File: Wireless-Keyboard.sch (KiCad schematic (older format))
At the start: 24 parts, among them SW1 SW_Push, U1 ATmega32U4-AU, Y1 16MHz

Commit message: schematic matrix done
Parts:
- added D? (x76): D_Small, Diode_SMD:D_SOD-123, symbol Device:D_Small
- added MX?: 2, MX_Only:MXOnly-1U-NoLED, symbol MX_Alps_Hybrid:MX-NoLED
- added MX?: W, MX_Only:MXOnly-1U-NoLED, symbol MX_Alps_Hybrid:MX-NoLED
- added MX?: 3, MX_Only:MXOnly-1U-NoLED, symbol MX_Alps_Hybrid:MX-NoLED
- added MX?: E, MX_Only:MXOnly-1U-NoLED, symbol MX_Alps_Hybrid:MX-NoLED
- added MX?: 4, MX_Only:MXOnly-1U-NoLED, symbol MX_Alps_Hybrid:MX-NoLED
- added MX?: R, MX_Only:MXOnly-1U-NoLED, symbol MX_Alps_Hybrid:MX-NoLED
- added MX?: 5, MX_Only:MXOnly-1U-NoLED, symbol MX_Alps_Hybrid:MX-NoLED
- added MX?: T, MX_Only:MXOnly-1U-NoLED, symbol MX_Alps_Hybrid:MX-NoLED
- added MX?: 6, MX_Only:MXOnly-1U-NoLED, symbol MX_Alps_Hybrid:MX-NoLED
- added MX?: Y, MX_Only:MXOnly-1U-NoLED, symbol MX_Alps_Hybrid:MX-NoLED
- added MX?: 7, MX_Only:MXOnly-1U-NoLED, symbol MX_Alps_Hybrid:MX-NoLED
- added MX?: U, MX_Only:MXOnly-1U-NoLED, symbol MX_Alps_Hybrid:MX-NoLED
- added MX?: 8, MX_Only:MXOnly-1U-NoLED, symbol MX_Alps_Hybrid:MX-NoLED
- added MX?: I, MX_Only:MXOnly-1U-NoLED, symbol MX_Alps_Hybrid:MX-NoLED
- added MX?: 9, MX_Only:MXOnly-1U-NoLED, symbol MX_Alps_Hybrid:MX-NoLED
- added MX?: O, MX_Only:MXOnly-1U-NoLED, symbol MX_Alps_Hybrid:MX-NoLED
- added MX?: 0, MX_Only:MXOnly-1U-NoLED, symbol MX_Alps_Hybrid:MX-NoLED
- added MX?: P, MX_Only:MXOnly-1U-NoLED, symbol MX_Alps_Hybrid:MX-NoLED
- added MX?: -_, MX_Only:MXOnly-1U-NoLED, symbol MX_Alps_Hybrid:MX-NoLED
- added MX?: [{, MX_Only:MXOnly-1U-NoLED, symbol MX_Alps_Hybrid:MX-NoLED
- added MX?: =+, MX_Only:MXOnly-1U-NoLED, symbol MX_Alps_Hybrid:MX-NoLED
- added MX?: ]}, MX_Only:MXOnly-1U-NoLED, symbol MX_Alps_Hybrid:MX-NoLED
- added MX?: Backspace 2u, MX_Only:MXOnly-1U-NoLED, symbol MX_Alps_Hybrid:MX-NoLED
- added MX?: Blank 3 1.5u, MX_Only:MXOnly-1U-NoLED, symbol MX_Alps_Hybrid:MX-NoLED
- added MX?: Blank 1 1u, MX_Only:MXOnly-1U-NoLED, symbol MX_Alps_Hybrid:MX-NoLED
- added MX? (x7): MX-NoLED, MX_Only:MXOnly-1U-NoLED, symbol MX_Alps_Hybrid:MX-NoLED
- added MX?: Blank 2 1u, MX_Only:MXOnly-1U-NoLED, symbol MX_Alps_Hybrid:MX-NoLED
- added MX?: A, MX_Only:MXOnly-1U-NoLED, symbol MX_Alps_Hybrid:MX-NoLED
- added MX?: CAPS 1.75u, MX_Only:MXOnly-1U-NoLED, symbol MX_Alps_Hybrid:MX-NoLED
- added MX?: S, MX_Only:MXOnly-1U-NoLED, symbol MX_Alps_Hybrid:MX-NoLED
- added MX?: D, MX_Only:MXOnly-1U-NoLED, symbol MX_Alps_Hybrid:MX-NoLED
- added MX?: F, MX_Only:MXOnly-1U-NoLED, symbol MX_Alps_Hybrid:MX-NoLED
- added MX?: G, MX_Only:MXOnly-1U-NoLED, symbol MX_Alps_Hybrid:MX-NoLED
- added MX?: H, MX_Only:MXOnly-1U-NoLED, symbol MX_Alps_Hybrid:MX-NoLED
- added MX?: J, MX_Only:MXOnly-1U-NoLED, symbol MX_Alps_Hybrid:MX-NoLED
- added MX?: K, MX_Only:MXOnly-1U-NoLED, symbol MX_Alps_Hybrid:MX-NoLED
- added MX?: L, MX_Only:MXOnly-1U-NoLED, symbol MX_Alps_Hybrid:MX-NoLED
- added MX?: ;:, MX_Only:MXOnly-1U-NoLED, symbol MX_Alps_Hybrid:MX-NoLED
- added MX?: @', MX_Only:MXOnly-1U-NoLED, symbol MX_Alps_Hybrid:MX-NoLED
- added MX?: Blank 4 2.25u, MX_Only:MXOnly-1U-NoLED, symbol MX_Alps_Hybrid:MX-NoLED
- added MX?: tilda#, MX_Only:MXOnly-1U-NoLED, symbol MX_Alps_Hybrid:MX-NoLED
- added MX?: ENTER ISO, MX_Only:MXOnly-1U-NoLED, symbol MX_Alps_Hybrid:MX-NoLED
- added MX?: \\|, MX_Only:MXOnly-1U-NoLED, symbol MX_Alps_Hybrid:MX-NoLED
- added MX?: LShift 1.25u, MX_Only:MXOnly-1U-NoLED, symbol MX_Alps_Hybrid:MX-NoLED
- added MX?: Blank 5 2.25u, MX_Only:MXOnly-1U-NoLED, symbol MX_Alps_Hybrid:MX-NoLED
- added MX?: Z, MX_Only:MXOnly-1U-NoLED, symbol MX_Alps_Hybrid:MX-NoLED
- added MX?: X, MX_Only:MXOnly-1U-NoLED, symbol MX_Alps_Hybrid:MX-NoLED
- added MX?: C, MX_Only:MXOnly-1U-NoLED, symbol MX_Alps_Hybrid:MX-NoLED
- added MX?: V, MX_Only:MXOnly-1U-NoLED, symbol MX_Alps_Hybrid:MX-NoLED
- added MX?: B, MX_Only:MXOnly-1U-NoLED, symbol MX_Alps_Hybrid:MX-NoLED
- added MX?: N, MX_Only:MXOnly-1U-NoLED, symbol MX_Alps_Hybrid:MX-NoLED
- added MX?: M, MX_Only:MXOnly-1U-NoLED, symbol MX_Alps_Hybrid:MX-NoLED
- added MX?: <,, MX_Only:MXOnly-1U-NoLED, symbol MX_Alps_Hybrid:MX-NoLED
- added MX?: .>, MX_Only:MXOnly-1U-NoLED, symbol MX_Alps_Hybrid:MX-NoLED
- added MX?: /?, MX_Only:MXOnly-1U-NoLED, symbol MX_Alps_Hybrid:MX-NoLED
- added MX?: RShift 2.75U, MX_Only:MXOnly-1U-NoLED, symbol MX_Alps_Hybrid:MX-NoLED
- added MX?: WIN 1.25U, MX_Only:MXOnly-1U-NoLED, symbol MX_Alps_Hybrid:MX-NoLED
- added MX?: LCTRL 1.25U, MX_Only:MXOnly-1U-NoLED, symbol MX_Alps_Hybrid:MX-NoLED
- added MX?: ALT 1.25U, MX_Only:MXOnly-1U-NoLED, symbol MX_Alps_Hybrid:MX-NoLED
- added MX? (x6): ***, MX_Only:MXOnly-1U-NoLED, symbol MX_Alps_Hybrid:MX-NoLED
- added MX?: SPACEBAR 6.25U, MX_Only:MXOnly-1U-NoLED, symbol MX_Alps_Hybrid:MX-NoLED
- added MX?: ALTGR 1.25u, MX_Only:MXOnly-1U-NoLED, symbol MX_Alps_Hybrid:MX-NoLED
- added MX?: WIN 1.25u, MX_Only:MXOnly-1U-NoLED, symbol MX_Alps_Hybrid:MX-NoLED
- added MX?: FN 1.25U, MX_Only:MXOnly-1U-NoLED, symbol MX_Alps_Hybrid:MX-NoLED
- added MX?: RCTRL 1.25u, MX_Only:MXOnly-1U-NoLED, symbol MX_Alps_Hybrid:MX-NoLED
- MX1: value MX-NoLED -> ESC; footprint (none) -> MX_Only:MXOnly-1U-NoLED
- MX2: value MX-NoLED -> Tab 1.5u; footprint (none) -> MX_Only:MXOnly-1U-NoLED
- MX3: value MX-NoLED -> 1; footprint (none) -> MX_Only:MXOnly-1U-NoLED
- MX4: value MX-NoLED -> Q; footprint (none) -> MX_Only:MXOnly-1U-NoLED
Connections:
- net labels added: COL10, COL11, COL12, COL13, COL14, COL15, COL2, COL3, COL4, COL5, COL6, COL7, COL8, COL9, ROW2, ROW3, ROW4
- wire segments 58 -> 286
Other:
- moved on the sheet: C1, C2, C3, C4, C5, C6, C7, D3, D4, MX3, MX4, R1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

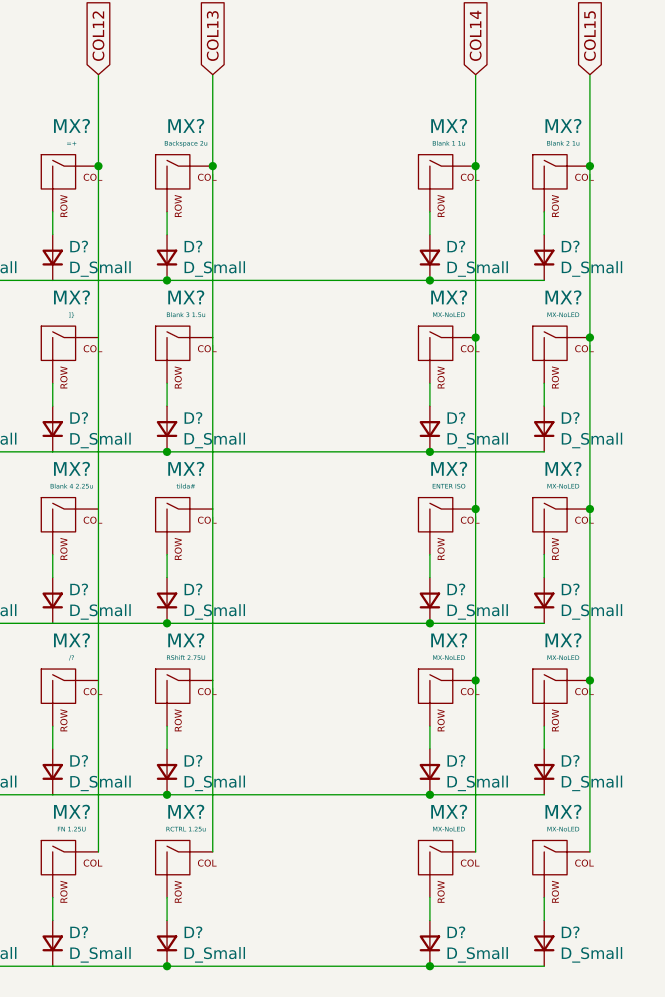
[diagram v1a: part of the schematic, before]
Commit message: Schematic redraw
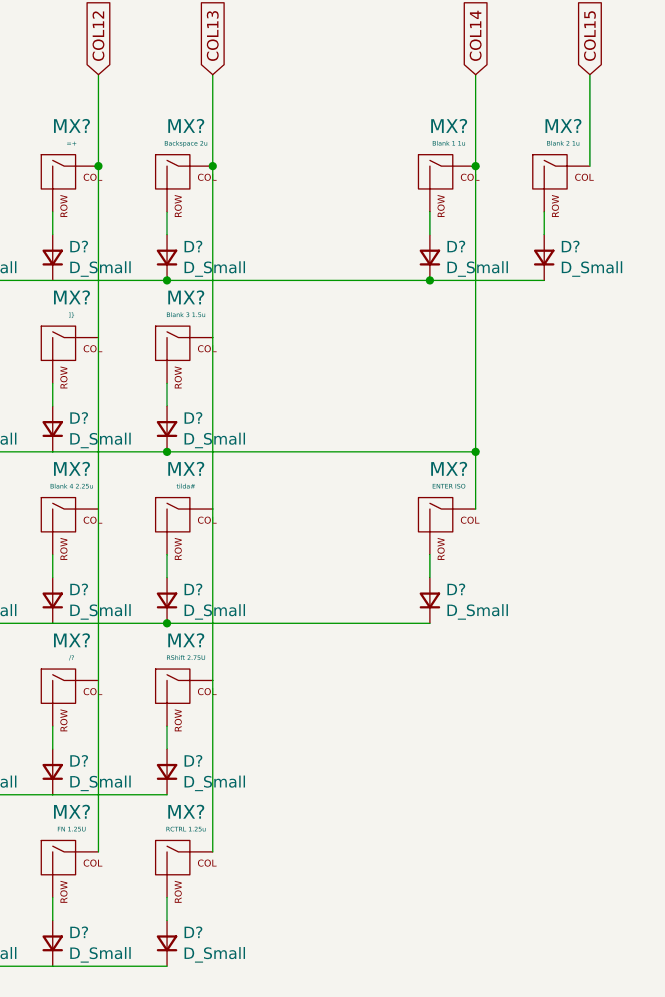
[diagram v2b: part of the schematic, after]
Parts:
- removed D? (x7): D_Small, Diode_SMD:D_SOD-123, symbol Device:D_Small
- removed MX? (x7): MX-NoLED, MX_Only:MXOnly-1U-NoLED, symbol MX_Alps_Hybrid:MX-NoLED
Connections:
- wire segments 286 -> 267
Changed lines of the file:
@@
-$EndComp
-$Comp
-L MX_Alps_Hybrid:MX-NoLED MX?
-U 1 1 5FA6B7BE
-P 14700 4650
-F 0 "MX?" H 14733 4873 60  0000 C CNN
-F 1 "MX-NoLED" H 14733 4799 20  0000 C CNN
-F 2 "MX_Only:MXOnly-1U-NoLED" H 14075 4625 60  0001 C CNN
-F 3 "" H 14075 4625 60  0001 C CNN
-	1    14700 4650
-	1    0    0    -1
-$EndComp
-$Comp
-L Device:D_Small D?
-U 1 1 5FA6B7C4
-P 14650 5000
-F 0 "D?" V 14696 4930 50  0000 R CNN
-F 1 "D_Small" V 14605 4930 50  0000 R CNN
-F 2 "Diode_SMD:D_SOD-123" V 14559 4930 50  0001 R CNN
-F 3 "~" V 14650 5000 50  0001 C CNN
-	1    14650 5000
-	0    -1   -1   0
 $EndComp
 $Comp
@@
 Wire Wire Line
 	14650 4050 14650 4150
-Wire Wire Line
-	14650 4800 14650 4900
-Wire Wire Line
-	14850 4600 14850 3850
 Connection ~ 14850 3850
 Wire Wire Line
@@
 $EndComp
 $Comp
-L MX_Alps_Hybrid:MX-NoLED MX?
-U 1 1 5FA6B7DE
-P 15200 4650
-F 0 "MX?" H 15233 4873 60  0000 C CNN
-F 1 "MX-NoLED" H 15233 4799 20  0000 C CNN
-F 2 "MX_Only:MXOnly-1U-NoLED" H 14575 4625 60  0001 C CNN
-F 3 "" H 14575 4625 60  0001 C CNN
-	1    15200 4650
-	1    0    0    -1
-$EndComp
-$Comp
-L Device:D_Small D?
-U 1 1 5FA6B7E4
-P 15150 5000
-F 0 "D?" V 15196 4930 50  0000 R CNN
-F 1 "D_Small" V 15105 4930 50  0000 R CNN
-F 2 "Diode_SMD:D_SOD-123" V 15059 4930 50  0001 R CNN
-F 3 "~" V 15150 5000 50  0001 C CNN
-	1    15150 5000
-	0    -1   -1   0
-$EndComp
-$Comp
 L Device:D_Small D?
 U 1 1 5FA6B7EA
@@
 	15150 4050 15150 4150
 Wire Wire Line
-	15150 4800 15150 4900
-Wire Wire Line
-	15350 4600 15350 3850
-Connection ~ 15350 3850
-Wire Wire Line
 	15350 3850 15350 3450
 Text GLabel 15350 3450 1    50   Input ~ 0
@@
 Wire Wire Line
 	15150 4350 14650 4350
-Wire Wire Line
-	15150 5100 14650 5100
 $Comp
 L MX_Alps_Hybrid:MX-NoLED MX?
@@
 Wire Wire Line
 	14650 5550 14650 5650
-Wire Wire Line
-	14850 5350 14850 4600
-$Comp
-L MX_Alps_Hybrid:MX-NoLED MX?
-U 1 1 5FAA31C5
-P 15200 5400
-F 0 "MX?" H 15233 5623 60  0000 C CNN
-F 1 "MX-NoLED" H 15233 5549 20  0000 C CNN
-F 2 "MX_Only:MXOnly-1U-NoLED" H 14575 5375 60  0001 C CNN
-F 3 "" H 14575 5375 60  0001 C CNN
-	1    15200 5400
-	1    0    0    -1
-$EndComp
-$Comp
-L Device:D_Small D?
-U 1 1 5FAA31CB
-P 15150 5750
-F 0 "D?" V 15196 5680 50  0000 R CNN
-F 1 "D_Small" V 15105 5680 50  0000 R CNN
-F 2 "Diode_SMD:D_SOD-123" V 15059 5680 50  0001 R CNN
-F 3 "~" V 15150 5750 50  0001 C CNN
-	1    15150 5750
-	0    -1   -1   0
-$EndComp
-Wire Wire Line
-	15150 5550 15150 5650
-Wire Wire Line
-	15350 5350 15350 4600
-Wire Wire Line
-	15150 5850 14650 5850
 $Comp
 L MX_Alps_Hybrid:MX-NoLED MX?
@@
 $Comp
 L MX_Alps_Hybrid:MX-NoLED MX?
-U 1 1 5FAB9719
-P 14700 6150
-F 0 "MX?" H 14733 6373 60  0000 C CNN
-F 1 "MX-NoLED" H 14733 6299 20  0000 C CNN
-F 2 "MX_Only:MXOnly-1U-NoLED" H 14075 6125 60  0001 C CNN
-F 3 "" H 14075 6125 60  0001 C CNN
-	1    14700 6150
-	1    0    0    -1
-$EndComp
-$Comp
-L Device:D_Small D?
-U 1 1 5FAB971F
-P 14650 6500
-F 0 "D?" V 14696 6430 50  0000 R CNN
-F 1 "D_Small" V 14605 6430 50  0000 R CNN
-F 2 "Diode_SMD:D_SOD-123" V 14559 6430 50  0001 R CNN
-F 3 "~" V 14650 6500 50  0001 C CNN
-	1    14650 6500
-	0    -1   -1   0
-$EndComp
-Wire Wire Line
-	14650 6300 14650 6400
-Wire Wire Line
-	14850 6100 14850 5350
-$Comp
-L MX_Alps_Hybrid:MX-NoLED MX?
-U 1 1 5FAB9728
-P 15200 6150
-F 0 "MX?" H 15233 6373 60  0000 C CNN
-F 1 "MX-NoLED" H 15233 6299 20  0000 C CNN
-F 2 "MX_Only:MXOnly-1U-NoLED" H 14575 6125 60  0001 C CNN
-F 3 "" H 14575 6125 60  0001 C CNN
-	1    15200 6150
-	1    0    0    -1
-$EndComp
-$Comp
-L Device:D_Small D?
-U 1 1 5FAB972E
-P 15150 6500
-F 0 "D?" V 15196 6430 50  0000 R CNN
-F 1 "D_Small" V 15105 6430 50  0000 R CNN
-F 2 "Diode_SMD:D_SOD-123" V 15059 6430 50  0001 R CNN
-F 3 "~" V 15150 6500 50  0001 C CNN
-	1    15150 6500
-	0    -1   -1   0
-$EndComp
-Wire Wire Line
-	15150 6300 15150 6400
-Wire Wire Line
-	15350 6100 15350 5350
-Wire Wire Line
-	15150 6600 14650 6600
-$Comp
-L MX_Alps_Hybrid:MX-NoLED MX?
 U 1 1 5FAE0A8F
 P 7550 6900
@@
 Wire Wire Line
 	13500 7350 13000 7350
-$Comp
-L MX_Alps_Hybrid:MX-NoLED MX?
-U 1 1 5FAE0B63
-P 14700 6900
-F 0 "MX?" H 14733 7123 60  0000 C CNN
-F 1 "MX-NoLED" H 14733 7049 20  0000 C CNN
-F 2 "MX_Only:MXOnly-1U-NoLED" H 14075 6875 60  0001 C CNN
-F 3 "" H 14075 6875 60  0001 C CNN
-	1    14700 6900
-	1    0    0    -1
-$EndComp
-$Comp
-L Device:D_Small D?
-U 1 1 5FAE0B69
-P 14650 7250
-F 0 "D?" V 14696 7180 50  0000 R CNN
-F 1 "D_Small" V 14605 7180 50  0000 R CNN
-F 2 "Diode_SMD:D_SOD-123" V 14559 7180 50  0001 R CNN
-F 3 "~" V 14650 7250 50  0001 C CNN
-	1    14650 7250
-	0    -1   -1   0
-$EndComp
-Wire Wire Line
-	14650 7050 14650 7150
-Wire Wire Line
-	14850 6850 14850 6100
-$Comp
-L MX_Alps_Hybrid:MX-NoLED MX?
-U 1 1 5FAE0B72
-P 15200 6900
-F 0 "MX?" H 15233 7123 60  0000 C CNN
-F 1 "MX-NoLED" H 15233 7049 20  0000 C CNN
-F 2 "MX_Only:MXOnly-1U-NoLED" H 14575 6875 60  0001 C CNN
-F 3 "" H 14575 6875 60  0001 C CNN
-	1    15200 6900
-	1    0    0    -1
-$EndComp
-$Comp
-L Device:D_Small D?
-U 1 1 5FAE0B78
-P 15150 7250
-F 0 "D?" V 15196 7180 50  0000 R CNN
-F 1 "D_Small" V 15105 7180 50  0000 R CNN
-F 2 "Diode_SMD:D_SOD-123" V 15059 7180 50  0001 R CNN
-F 3 "~" V 15150 7250 50  0001 C CNN
-	1    15150 7250
-	0    -1   -1   0
-$EndComp
-Wire Wire Line
-	15150 7050 15150 7150
-Wire Wire Line
-	15350 6850 15350 6100
-Wire Wire Line
-	15150 7350 14650 7350
 Connection ~ 14650 4350
-Connection ~ 14650 5100
-Connection ~ 14650 5850
-Connection ~ 14650 6600
-Connection ~ 14650 7350
-Connection ~ 14850 4600
-Connection ~ 14850 5350
-Connection ~ 14850 6100
-Connection ~ 15350 4600
-Connection ~ 15350 5350
-Connection ~ 15350 6100
 Wire Wire Line
 	13500 4350 14650 4350
 Connection ~ 13500 4350
 Wire Wire Line
-	13500 5100 14650 5100
-Connection ~ 13500 5100
-Wire Wire Line
 	13500 5850 14650 5850
 Connection ~ 13500 5850
 Wire Wire Line
-	13500 6600 14650 6600
-Connection ~ 13500 6600
-Wire Wire Line
-	13500 7350 14650 7350
-Connection ~ 13500 7350
+	14850 3850 14850 5100
+Wire Wire Line
+	13500 5100 14850 5100
+Connection ~ 13500 5100
+Connection ~ 14850 5100
+Wire Wire Line
+	14850 5100 14850 5350
 $EndSCHEMATC

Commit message: keymap layout finished
finish the keymap layout. waiting to place all the component and eventually finish traces
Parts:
- removed D? (x9): D_Small, Diode_SMD:D_SOD-123, symbol Device:D_Small
- removed F1: 500mA, Fuse:Fuse_1206_3216Metric, symbol Device:Polyfuse_Small
- removed MX?: Blank 5 2.25u, MX_Only:MXOnly-1U-NoLED, symbol MX_Alps_Hybrid:MX-NoLED
- removed MX? (x5): ***, MX_Only:MXOnly-1U-NoLED, symbol MX_Alps_Hybrid:MX-NoLED
- removed MX?: FN 1.25U, MX_Only:MXOnly-1U-NoLED, symbol MX_Alps_Hybrid:MX-NoLED
- removed USB1: Molex-0548190589, random-keyboard-parts:Molex-0548190589, symbol random-keyboard-parts:Molex-0548190589
- removed Y1: 16MHz, Crystal:Crystal_SMD_3225-4Pin_3.2x2.5mm, symbol Device:Crystal_GND24_Small
- added D59: D_Small, Diode_SMD:D_SOD-123, symbol Device:D_Small
- added F1: Polyfuse, Fuse:Fuse_1206_3216Metric, symbol Device:Polyfuse
- added MX31: step cap 1.75u, MX_Only:MXOnly-1U-NoLED, symbol MX_Alps_Hybrid:MX-NoLED
- added MX47: iso leftshift 1.25u, MX_Only:MXOnly-1.25U-NoLED, symbol MX_Alps_Hybrid:MX-NoLED
- added MX62: RShift 1.75U, MX_Only:MXOnly-1.75U-NoLED, symbol MX_Alps_Hybrid:MX-NoLED
- added MX63: DEL 1U, MX_Only:MXOnly-1U-NoLED, symbol MX_Alps_Hybrid:MX-NoLED
- added R4, R5: 5.1k, Resistor_SMD:R_0805_2012Metric, symbol Device:R_Small
- added U1: PRTR5V0U2X, local:SOT143B, symbol ai03_keyboard_parts:PRTR5V0U2X
- added USB1: HRO-TYPE-C-31-M-12, typec:HRO-TYPE-C-31-M-12-Assembly, symbol typ-c:HRO-TYPE-C-31-M-12
- added Y1: 16Mhz, Crystal:Crystal_SMD_3225-4Pin_3.2x2.5mm, symbol Device:Crystal_GND24
- MX14: renamed from MX?; footprint MX_Only:MXOnly-1U-NoLED -> MX_Only:MXOnly-2U-NoLED
- MX17: renamed from MX2; footprint MX_Only:MXOnly-1U-NoLED -> MX_Only:MXOnly-1.5U-NoLED
- MX30: renamed from MX?; value Blank 3 1.5u -> \\ 1.5u; footprint MX_Only:MXOnly-1U-NoLED -> MX_Only:MXOnly-1.5U-NoLED
- MX32: renamed from MX?; footprint MX_Only:MXOnly-1U-NoLED -> MX_Only:MXOnly-1.75U-NoLED
- MX43: renamed from MX?; value @' -> '\"
- MX44: renamed from MX?; value Blank 4 2.25u -> iso tilda 1u
- MX45: renamed from MX?; value tilda# -> enter 2.25u; footprint MX_Only:MXOnly-1U-NoLED -> MX_Only:MXOnly-2.25U-NoLED
- MX46: renamed from MX?; footprint MX_Only:MXOnly-1U-NoLED -> MX_Only:MXOnly-ISO-ROTATED-ReversedStabilizers-NoLED
- MX48: renamed from MX?; value LShift 1.25u -> LShift 2.25u; footprint MX_Only:MXOnly-1U-NoLED -> MX_Only:MXOnly-2.25U-NoLED
- MX61: renamed from MX?; footprint MX_Only:MXOnly-1U-NoLED -> MX_Only:MXOnly-2.75U-NoLED
- MX64, MX65, MX66, MX71: renamed from MX?; footprint MX_Only:MXOnly-1U-NoLED -> MX_Only:MXOnly-1.25U-NoLED
- MX67: renamed from MX?; footprint MX_Only:MXOnly-1U-NoLED -> MX_Only:MXOnly-6.25U-ReversedStabilizers-NoLED
- MX68: renamed from MX?; value *** -> RALT1.25U; footprint MX_Only:MXOnly-1U-NoLED -> MX_Only:MXOnly-1.25U-NoLED
- MX69: renamed from MX?; value ALTGR 1.25u -> RWIN1.25U; footprint MX_Only:MXOnly-1U-NoLED -> MX_Only:MXOnly-1.25U-NoLED
- MX70: renamed from MX?; value WIN 1.25u -> FN1.25U; footprint MX_Only:MXOnly-1U-NoLED -> MX_Only:MXOnly-1.25U-NoLED
- gave numbers to parts that had none: 105
- renumbered C4 to C1, C5 to C2, C7 to C3, C1 to C4, C2 to C5, C3 to C6, C6 to C7, D2 to D16, D4 to D17, D3 to D2, MX4 to MX18, MX3 to MX2, R4 to R6, U1 to U2
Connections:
- net labels removed: COL15
- wire segments 267 -> 289
- no-connect marks 0 -> 8
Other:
- moved on the sheet: C1, C2, D15, D48, D49, D50, D51, D52, D53, D54, D55, D56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

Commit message: wiring for keymap mostly done. waiting for bluetooth module implementation
wiring for the keymap is mostly done,
TODO:
wiring for resistor, capacitor and crystal
implementation of the bluetooth module
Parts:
- added U2: MDBT40, symbol RF_Modules:MDBT40
- MX48: footprint MX_Only:MXOnly-2.25U-NoLED -> MX_Only:MXOnly-1U-NoLED
- U3: renamed from U1; symbol ai03_keyboard_parts:PRTR5V0U2X -> Wireless-Keyboard-rescue:PRTR5V0U2X-ai03_keyboard_parts
- USB1: symbol typ-c:HRO-TYPE-C-31-M-12 -> Wireless-Keyboard-rescue:HRO-TYPE-C-31-M-12-typ-c
- renumbered D45 to D44, D46 to D45, D48 to D46, D49 to D47, D50 to D48, D51 to D49, D52 to D50, D53 to D51, D54 to D52, D55 to D53, D56 to D54, D57 to D55, D58 to D56, D59 to D57, D60 to D58, D61 to D59, D62 to D60, D63 to D61, D64 to D62, D65 to D63, D66 to D64, D67 to D65, MX51 to MX50, MX52 to MX51, MX53 to MX52, MX54 to MX53, MX55 to MX54, MX56 to MX55, MX57 to MX56, MX58 to MX57, MX59 to MX58, MX60 to MX59, MX61 to MX60, MX62 to MX61, MX63 to MX62, MX64 to MX63, MX65 to MX64, MX66 to MX65, MX67 to MX66, MX68 to MX67, MX69 to MX68, MX70 to MX69, MX71 to MX70, R3 to R1, R6 to R2, R1 to R3, R2 to R4, R4 to R5, R5 to R6, U2 to U1
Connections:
- wire segments 289 -> 299
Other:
- moved on the sheet: D14, D15, D29, D43, D57, F1, MX14, MX15, MX16, MX30, MX31, MX45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

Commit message: USB connector wiring done
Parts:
- U2: symbol RF_Modules:MDBT40 -> Wireless-Keyboard-rescue:MDBT40-RF_Modules
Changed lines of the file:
@@
 Connection ~ 7700 6100
 $Comp
-L RF_Modules:MDBT40 U2
+L Wireless-Keyboard-rescue:MDBT40-RF_Modules U2
 U 1 1 5FAAA71F
 P 2975 9475

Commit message: Finished wiring except bluetooth implementaion
the general wiring for current design is finished. only need to implement the bluetooth module
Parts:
- U2: symbol Wireless-Keyboard-rescue:MDBT40-RF_Modules -> RF_Modules:MDBT40
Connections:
- net COL0: now also U1.22 (PD5); no longer U1.8 (PB0)
- net COL1: now also U1.21 (PD3); no longer U1.41 (PF0)
- net COL12: now also U1.37 (PF6); no longer U1.18 (PD0)
- net COL13: now also U1.36 (PF7); no longer U1.19 (PD1)
- net COL14: now also U1.41 (PF0); no longer U1.20 (PD2)
- net COL2: now also U1.20 (PD2); no longer U1.9 (PB1)
- net COL3: now also U1.19 (PD1); no longer U1.10 (PB2)
- net COL4: now also U1.18 (PD0); no longer U1.11 (PB3)
- net COL5: now also U1.26 (PD6); no longer U1.28 (PB4)
- net COL6: now also U1.27 (PD7); no longer U1.29 (PB5)
- net COL7: now also U1.28 (PB4); no longer U1.1 (PE6)
- net COL8: now also U1.29 (PB5); no longer U1.30 (PB6)
- net COL9: now also U1.30 (PB6); no longer U1.12 (PB7)
- net ROW0: now also U1.40 (PF1); no longer U1.21 (PD3)
- net ROW1: now also U1.39 (PF4); no longer U1.25 (PD4)
- net ROW2: now also U1.38 (PF5); no longer U1.22 (PD5)
- net ROW3: now also U1.25 (PD4); no longer U1.26 (PD6)
- net ROW4: now also U1.1 (PE6); no longer U1.27 (PD7)
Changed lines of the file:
@@
 Text GLabel 7700 3450 1    50   Input ~ 0
 COL1
-Text GLabel 3600 2300 2    50   Input ~ 0
+Text GLabel 3600 3600 2    50   Input ~ 0
 COL2
-Text GLabel 3600 2200 2    50   Input ~ 0
+Text GLabel 3600 3900 2    50   Input ~ 0
 COL0
-Text GLabel 3600 2800 2    50   Input ~ 0
+Text GLabel 3600 2700 2    50   Input ~ 0
 COL8
-Text GLabel 3600 4100 2    50   Input ~ 0
+Text GLabel 3600 4400 2    50   Input ~ 0
 ROW4
 Wire Notes Line
@@
 	-1   0    0    1
 $EndComp
-Text GLabel 3600 2400 2    50   Input ~ 0
+Text GLabel 3600 3500 2    50   Input ~ 0
 COL3
-Text GLabel 3600 2500 2    50   Input ~ 0
+Text GLabel 3600 3400 2    50   Input ~ 0
 COL4
-Text GLabel 3600 2600 2    50   Input ~ 0
+Text GLabel 3600 4000 2    50   Input ~ 0
 COL5
-Text GLabel 3600 2700 2    50   Input ~ 0
+Text GLabel 3600 4100 2    50   Input ~ 0
 COL6
-Text GLabel 3600 2900 2    50   Input ~ 0
+Text GLabel 3600 2800 2    50   Input ~ 0
 COL9
 Text GLabel 3600 3100 2    50   Input ~ 0
@@
 Text GLabel 3600 3200 2    50   Input ~ 0
 COL11
-Text GLabel 3600 3400 2    50   Input ~ 0
+Text GLabel 3600 5000 2    50   Input ~ 0
 COL12
-Text GLabel 3600 3500 2    50   Input ~ 0
+Text GLabel 3600 5100 2    50   Input ~ 0
 COL13
-Text GLabel 3600 3600 2    50   Input ~ 0
+Text GLabel 3600 4600 2    50   Input ~ 0
 COL14
+Text GLabel 3600 4700 2    50   Input ~ 0
+ROW0
+Text GLabel 3600 4800 2    50   Input ~ 0
+ROW1
+Text GLabel 3600 4900 2    50   Input ~ 0
+ROW2
+Text GLabel 3600 3800 2    50   Input ~ 0
+ROW3
+NoConn ~ 3600 2500
+NoConn ~ 3600 2400
+NoConn ~ 3600 2900
+NoConn ~ 3600 2200
+NoConn ~ 3600 2300
+Text GLabel 3600 2600 2    50   Input ~ 0
+COL7
 Text GLabel 3600 3700 2    50   Input ~ 0
-ROW0
-Text GLabel 3600 3800 2    50   Input ~ 0
-ROW1
-Text GLabel 3600 3900 2    50   Input ~ 0
-ROW2
-Text GLabel 3600 4000 2    50   Input ~ 0
-ROW3
-NoConn ~ 3600 4700
-NoConn ~ 3600 4800
-NoConn ~ 3600 4900
-NoConn ~ 3600 5000
-NoConn ~ 3600 5100
-Text GLabel 3600 4400 2    50   Input ~ 0
-COL7
-Text GLabel 3600 4600 2    50   Input ~ 0
 COL1
 Connection ~ 8000 6600
@@
 Connection ~ 7700 6100
 $Comp
-L Wireless-Keyboard-rescue:MDBT40-RF_Modules U2
+L RF_Modules:MDBT40 U2
 U 1 1 5FAAA71F
 P 2975 9475
